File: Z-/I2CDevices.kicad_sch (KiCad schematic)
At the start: 36 parts, among them U1 OPT4003DNPRQ1, U2 LTC4316xDD, U3 ADM1176-1ARMZ-R7, U4 NCV891330PD50R2G, U5 DRV8830DRC

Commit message: Z- Board Files
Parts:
- added R69, R70: 0R (DNI), Resistor_SMD:R_0603_1608Metric, symbol SolarPanels:R_Small
- added R71, R72: 0R, Resistor_SMD:R_0402_1005Metric, symbol SolarPanels:R_Small
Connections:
- net SCLOUT: now also R69.2, R72.1
- net SCL_LS: now also R69.1
- net SDAOUT: now also R70.2, R71.2
- net SDA_LS: now also R70.1
- net SW: now reaches C11.2, D2.1 (K), L1.1, U4.8 (SW)
- net ADDR: now reaches R25.1, R26.2, U1.2 (ADDR)
- net ADDR: now also R71.1, R72.2
- net VBATT renamed VBATT_SENSE
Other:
- note added: "Buck Regulator 5V"
- note added: "I2C ADDR Install R25: 0x45 Install R26: 0x44"
- note removed: "I2C ADDR Install R34: 0x45 Install R35: 0x44"
- moved on the sheet: D1

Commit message: Z- Solar Panel files upload
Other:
- moved on the sheet: C10, C11, C12, C13, C14, C15, C17, C5, C6, C7, C8, C9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

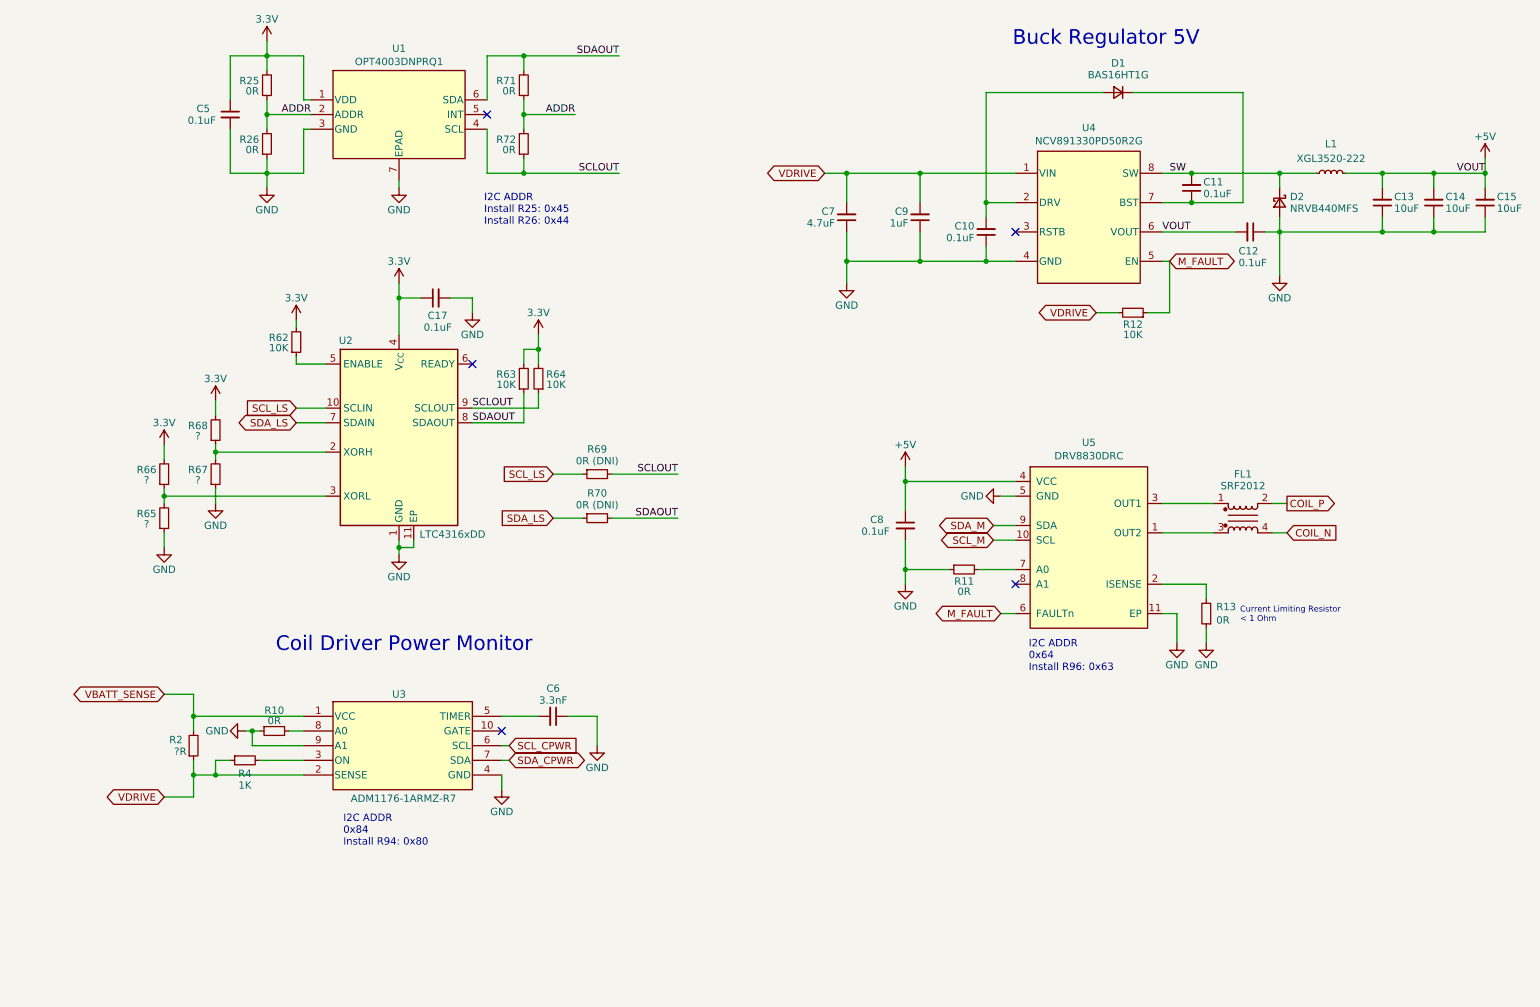
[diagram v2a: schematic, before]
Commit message: Added i2c expander for burnwires, reformatted i2c protection, swapped to drv8235
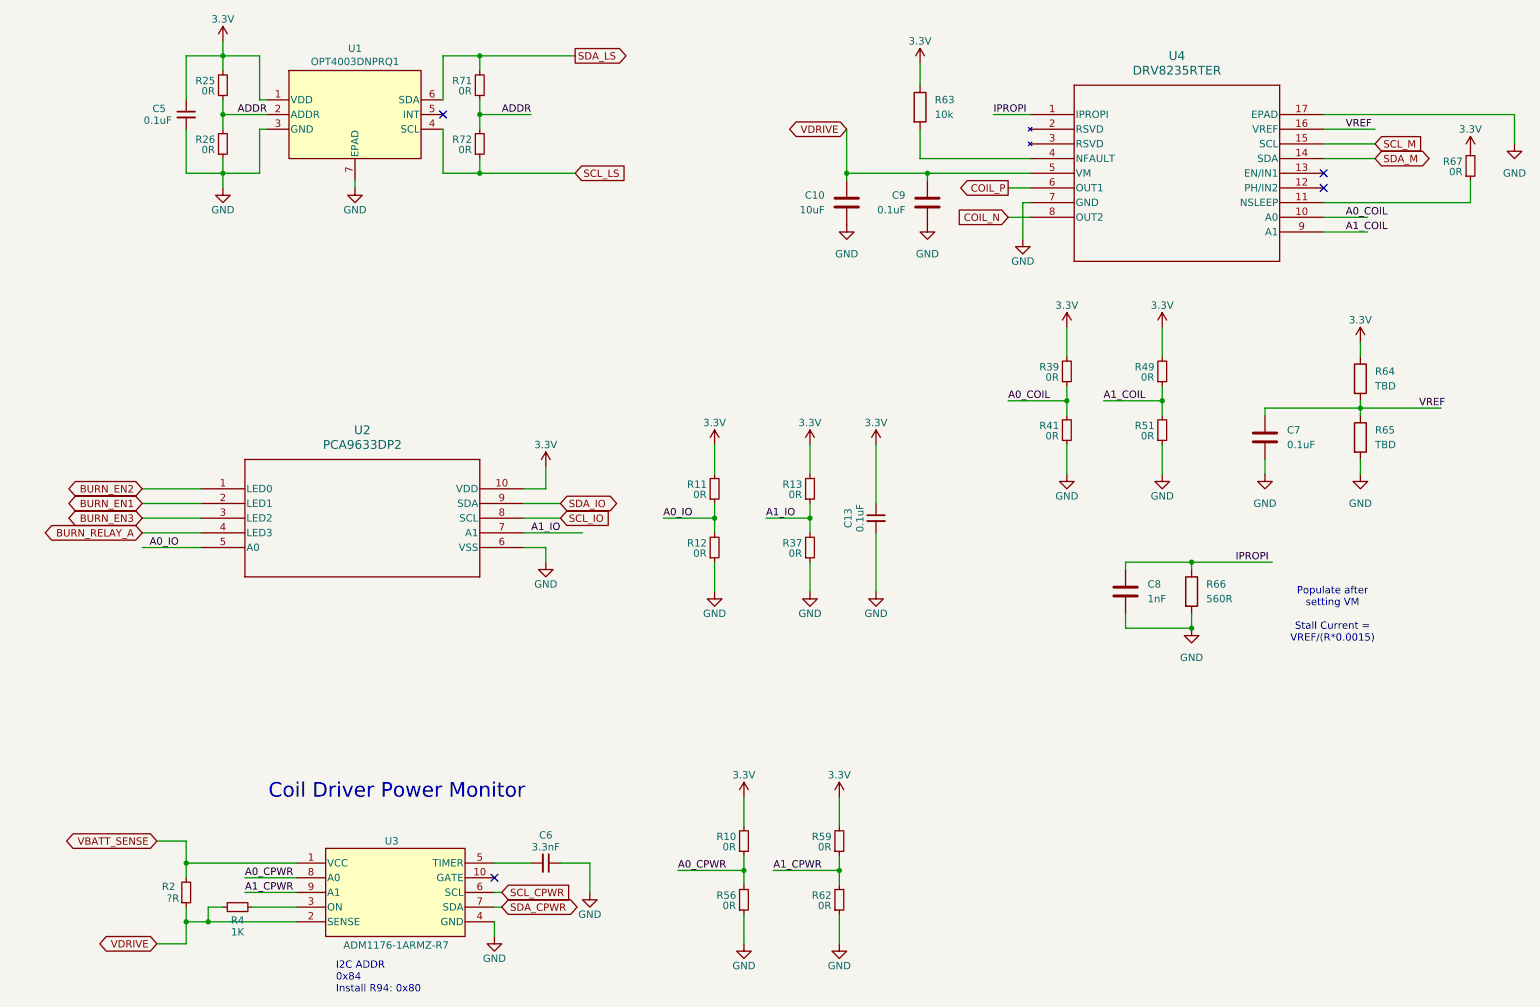
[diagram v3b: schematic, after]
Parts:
- removed C10, C11, C12, C17: 0.1uF, Capacitor_SMD:C_0603_1608Metric, symbol SolarPanels:C_Small
- removed C14, C15: 10uF, Capacitor_SMD:C_1206_3216Metric, symbol SolarPanels:C_Small
- removed C7: 4.7uF, Capacitor_SMD:C_1210_3225Metric, symbol SolarPanels:C_Small
- removed C8: 0.1uF, Capacitor_SMD:C_0805_2012Metric, symbol SolarPanels:C_Small
- removed C9: 1uF, Capacitor_SMD:C_0805_2012Metric, symbol SolarPanels:C_Small
- removed D1: BAS16HT1G, Diode_SMD:D_SOD-323, symbol SolarPanels:D_Small
- removed D2: NRVB440MFS, SolarPanels:NRVB440MFSWFT1G, symbol SolarPanels:D_Schottky_Small
- removed FL1: SRF2012, SolarPanels:SRF2012, symbol SolarPanels:Filter_EMI_CommonMode
- removed L1: XGL3520-222, SolarPanels:XGL3520, symbol SolarPanels:L_Small
- removed R63, R64: 10K, Resistor_SMD:R_0603_1608Metric, symbol SolarPanels:R_Small
- removed R65, R66, R68: ?, Resistor_SMD:R_0603_1608Metric, symbol SolarPanels:R_Small
- removed R69, R70: 0R (DNI), Resistor_SMD:R_0603_1608Metric, symbol SolarPanels:R_Small
- removed U2: LTC4316xDD, Package_DFN_QFN:DFN-10-1EP_3x3mm_P0.5mm_EP1.65x2.38mm, symbol Interface_Expansion:LTC4316xDD
- removed U4: NCV891330PD50R2G, Package_SO:SOIC-8-1EP_3.9x4.9mm_P1.27mm_EP2.514x3.2mm, symbol SolarPanels:NCV891330PD50R2G
- removed U5: DRV8830DRC, Package_SON:VSON-10-1EP_3x3mm_P0.5mm_EP1.65x2.4mm, symbol SolarPanels:DRV8830DRC
- added C10: 10uF, Capacitor_SMD:C_1206_3216Metric, symbol Device:C
- added C7, C9: 0.1uF, Capacitor_SMD:C_0603_1608Metric, symbol Device:C
- added C8: 1nF, Capacitor_SMD:C_0603_1608Metric, symbol Device:C
- added R37, R39, R41, R49, R51, R56, R59: 0R, Resistor_SMD:R_0603_1608Metric, symbol SolarPanels:R_Small
- added R63: 10k, Resistor_SMD:R_0603_1608Metric, symbol Device:R
- added R64, R65: TBD, Resistor_SMD:R_0603_1608Metric, symbol Device:R
- added R66: 560R, Resistor_SMD:R_0603_1608Metric, symbol Device:R
- added U2: PCA9633DP2, SOT552-1_NXP, symbol SolarPanels:PCA9633DP2
- added U4: DRV8235RTER, WQFN16_RTE_TEX, symbol SolarPanels:DRV8235RTER
- C13: value 10uF -> 0.1uF; footprint Capacitor_SMD:C_1206_3216Metric -> Capacitor_SMD:C_0603_1608Metric
- C5: footprint Capacitor_SMD:C_0402_1005Metric -> Capacitor_SMD:C_0603_1608Metric
- R12, R62: value 10K -> 0R
- R25, R26, R71, R72: footprint Resistor_SMD:R_0402_1005Metric -> Resistor_SMD:R_0603_1608Metric
- R67: value ? -> 0R
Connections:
- net +5V is gone; now on net GND: C13.2
- net M_FAULT is gone; now on net GND: R12.1
- net SCLOUT is gone; now on net SCL_LS: R72.1, U1.4 (SCL)
- net SDAOUT is gone; now on net SDA_LS: R71.2, U1.6 (SDA)
- net 3.3V: now also C13.1, R10.2, R11.2, R13.2, R67.2, R39.2, R49.2, R59.2, R63.1, R64.1, U2.10 (VDD); no longer R62.2
- net COIL_N: now also U4.8 (OUT2)
- net COIL_P: now also U4.6 (OUT1)
- net GND: now also R62.1, C10.2, C7.2, C8.2, C9.2, R37.1, R41.1, R51.1, R56.1, R65.2, R66.2, U2.6 (VSS), U4.17 (EPAD), U4.7 (GND); no longer C13.1, R10.1, R11.1, R13.1, R67.1, U3.9 (A1)
- net SCL_M: now also U4.15 (SCL)
- net SDA_M: now also U4.14 (SDA)
- net VDRIVE: now also C10.1, C9.1, U4.5 (VM); no longer R12.2
- net A0_CPWR: now reaches U3.8 (A0)
- net A0_CPWR: now also R10.1, R56.2; no longer R10.2
- new net: R67.1, U4.11 (NSLEEP)
- new net: R63.2, U4.4 (NFAULT)
- new net A0_COIL: R39.1, R41.2, U4.10 (A0)
- new net A0_IO: R11.1, R12.2, U2.5 (A0)
- new net A1_COIL: R49.1, R51.2, U4.9 (A1)
- new net A1_CPWR: R59.1, R62.2, U3.9 (A1)
- new net A1_IO: R13.1, R37.2, U2.7 (A1)
- new net BURN_EN1: U2.2 (LED1)
- new net BURN_EN2: U2.1 (LED0)
- new net BURN_EN3: U2.3 (LED2)
- new net BURN_RELAY_A: U2.4 (LED3)
- new net IPROPI: C8.1, R66.1, U4.1 (IPROPI)
- new net SCL_IO: U2.8 (SCL)
- new net SDA_IO: U2.9 (SDA)
- new net VREF: C7.1, R64.2, R65.1, U4.16 (VREF)
- no-connect marks 5 -> 4
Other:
- note added: "Populate after setting VM Stall Current = VREF/(R*0.0015)"
- note removed: "Buck Regulator 5V"
- note removed: "Current Limiting Resistor < 1 Ohm"
- note removed: "I2C ADDR 0x64 Install R96: 0x63"
- note removed: "I2C ADDR Install R25: 0x45 Install R26: 0x44"
- moved on the sheet: C5, C6, R2, R25, R26, R4, R71, R72, U1, U3

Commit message: Moved burnwire around and added switch to coil driver
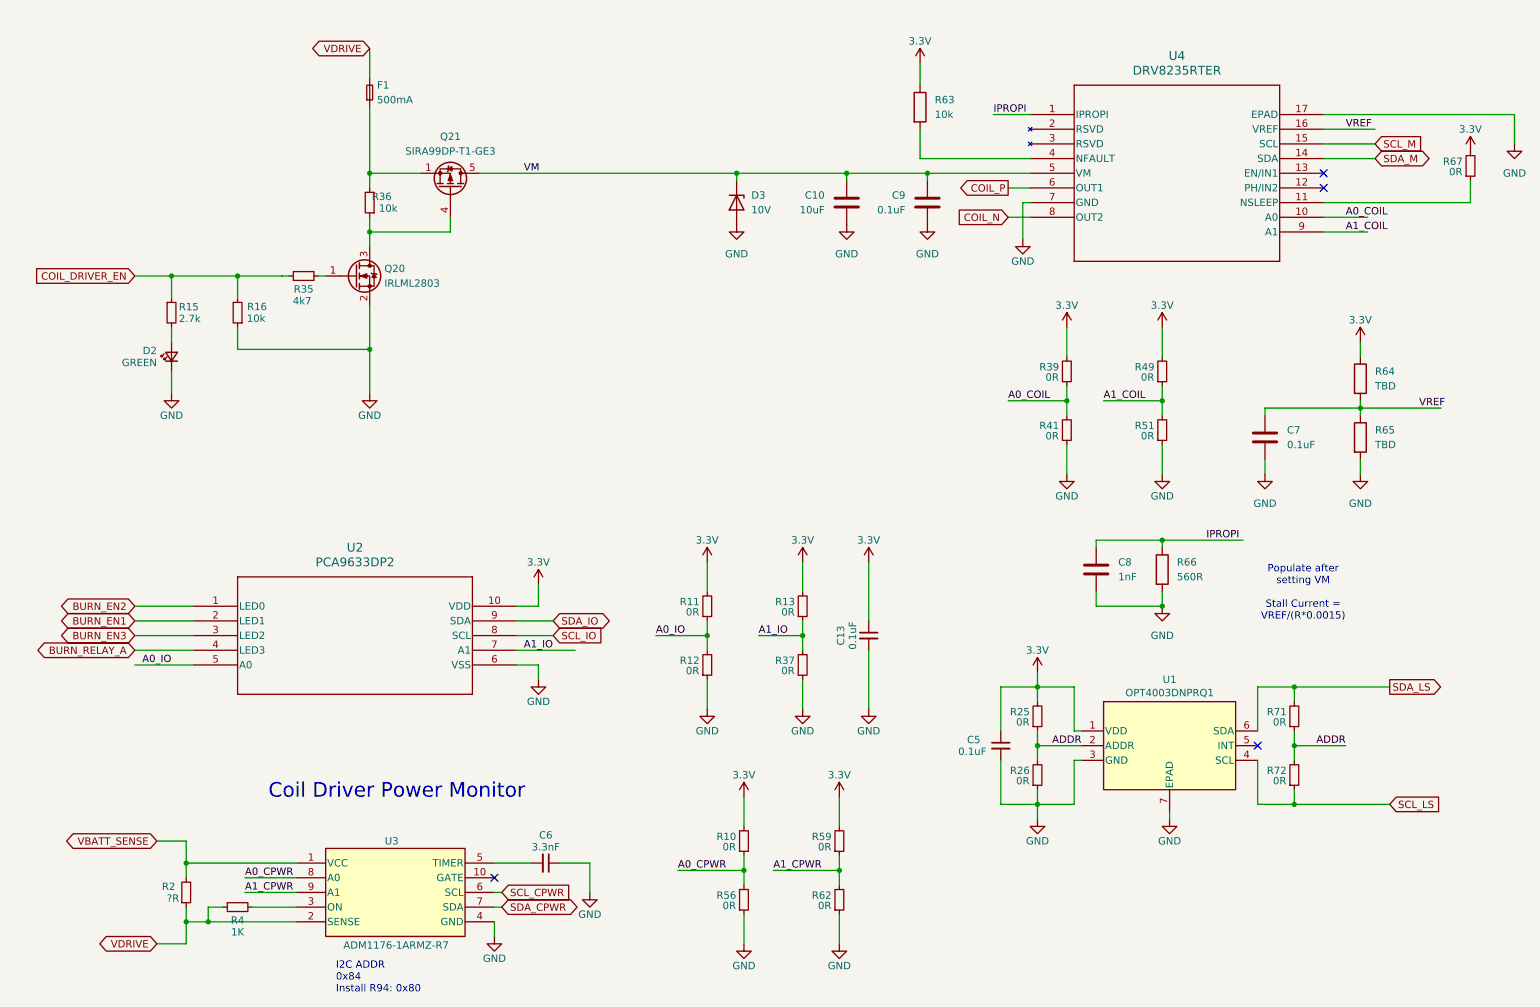
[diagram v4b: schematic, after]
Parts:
- added D2: GREEN, LED_SMD:LED_0603_1608Metric, symbol Device:LED_Small
- added D3: 10V, Diode_SMD:Nexperia_DSN1608-2_1.6x0.8mm, symbol Diode:PTVS10VZ1USK
- added F1: 500mA, Fuse:Fuse_0603_1608Metric, symbol Device:Fuse_Small
- added Q20: IRLML2803, Package_TO_SOT_SMD:SOT-23, symbol Argus-IC:IRLML2803
- added Q21: SIRA99DP-T1-GE3, Package_SO:PowerPAK_SO-8_Single, symbol Transistor_FET:Si7141DP
- added R15: 2.7k, Resistor_SMD:R_0603_1608Metric, symbol Device:R_Small
- added R16, R36: 10k, Resistor_SMD:R_0603_1608Metric, symbol Device:R_Small
- added R35: 4k7, Resistor_SMD:R_0603_1608Metric, symbol Device:R_Small
- C13, C5, C6: symbol SolarPanels:C_Small -> Device:C_Small
- R10, R11, R12, R13, R2, R25, R26, R37, R39, R4, R41, R49, R51, R56, R59, R62, R67, R71, R72: symbol SolarPanels:R_Small -> Device:R_Small
- U1: footprint SolarPanels:OPT4003 -> Argus-IC:OPT4003; symbol SolarPanels:OPT4003DNPRQ1 -> Argus-IC:OPT4003DNPRQ1
- U2: footprint SOT552-1_NXP -> Argus-IC:SOT552-1_NXP; symbol SolarPanels:PCA9633DP2 -> Argus-IC:PCA9633DP2
- U3: symbol SolarPanels:ADM1176-1ARMZ-R7 -> Argus-IC:ADM1176-1ARMZ-R7
- U4: footprint WQFN16_RTE_TEX -> Argus-IC:WQFN16_RTE_TEX; symbol SolarPanels:DRV8235RTER -> Argus-IC:DRV8235RTER
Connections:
- net GND: now also D2.1 (K), D3.2 (A), Q20.2 (S), R16.1
- net VDRIVE: now also F1.2; no longer C10.1, C9.1, U4.5 (VM)
- new net: D2.2 (A), R15.2
- new net: Q20.1 (G), R35.2
- new net: Q20.3 (D), Q21.4 (G), R36.1
- new net: F1.1, Q21.1 (S), Q21.2 (S), Q21.3 (S), R36.2
- new net COIL_DRIVER_EN: R15.1, R16.2, R35.1
- new net VM: C10.1, C9.1, D3.1 (K), Q21.5 (D), U4.5 (VM)
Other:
- moved on the sheet: C13, C5, C8, R11, R12, R13, R25, R26, R37, R66, R71, R72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

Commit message: Started adding main/peripheral 3v3 nets
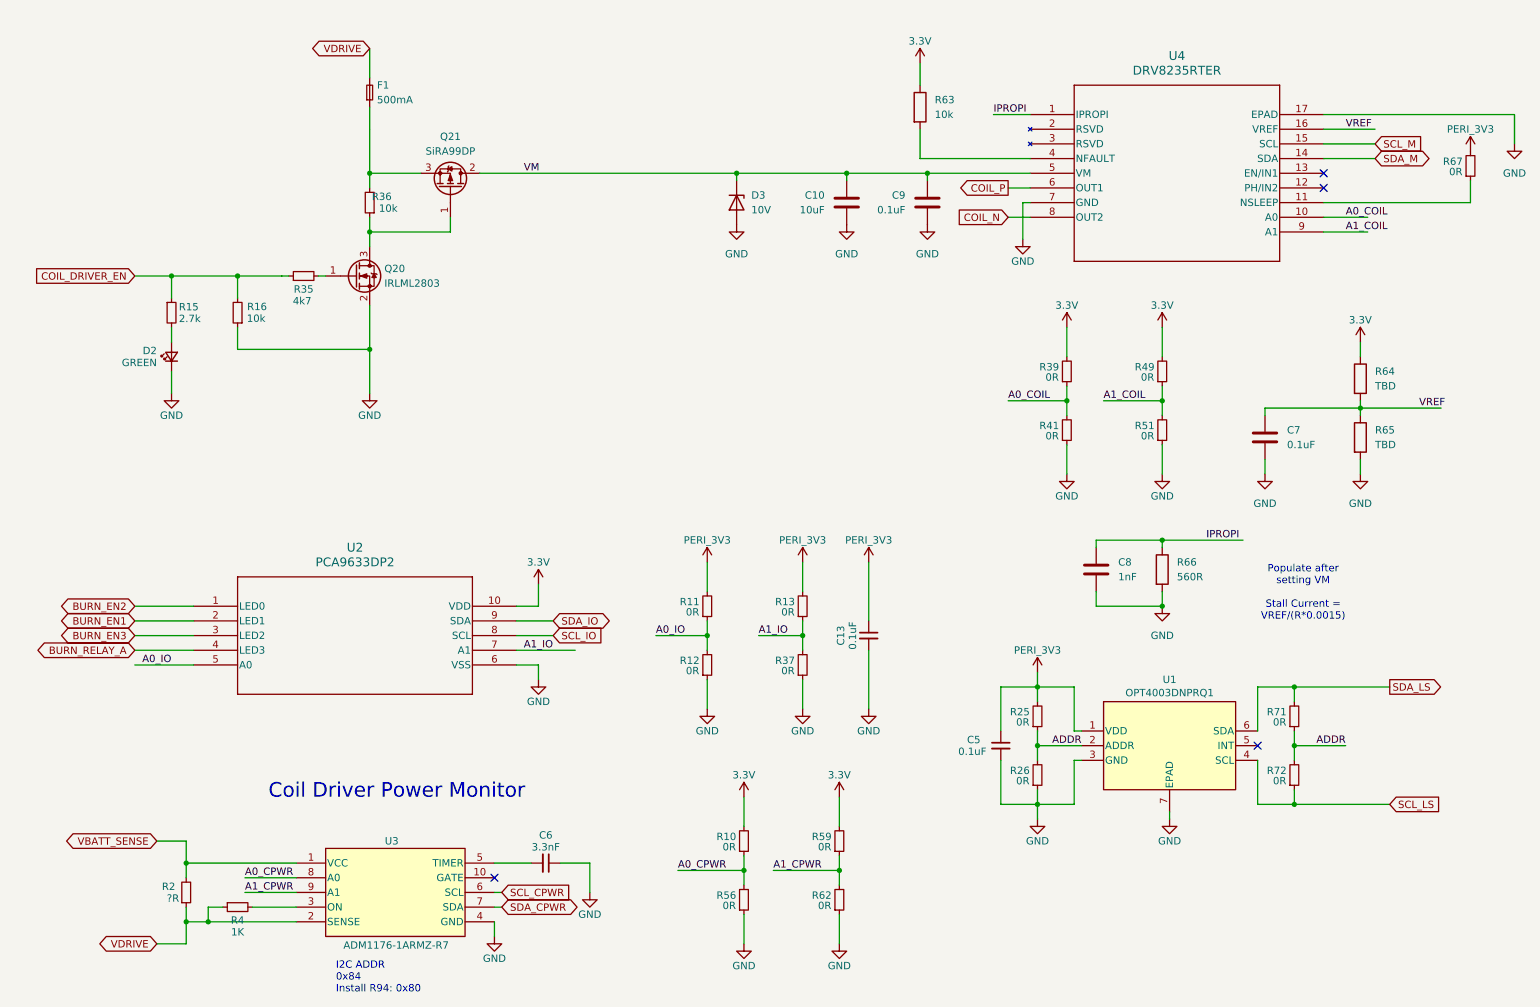
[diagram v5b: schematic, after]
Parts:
- removed Q21: SIRA99DP-T1-GE3, Package_SO:PowerPAK_SO-8_Single, symbol Transistor_FET:Si7141DP
- added Q21: SiRA99DP, Argus-Miscellaneous:PowerPAK SO-8, symbol Argus-IC:Q_PMOS_GDS
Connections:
- net 3.3V: no longer C13.1, C5.1, R11.2, R13.2, R25.2, R67.2, U1.1 (VDD)
- net VM: now also Q21.2 (D)
- net at Q20.3 (D), R36.1: now also Q21.1 (G)
- net at F1.1, R36.2: now also Q21.3 (S)
- new net PERI_3V3: C13.1, C5.1, R11.2, R13.2, R25.2, R67.2, U1.1 (VDD)
